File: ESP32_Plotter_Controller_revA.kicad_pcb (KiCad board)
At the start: 2 copper layers, 99.1 x 55.4 mm, 40 parts, among them J1 ARM JTAG 10pin, J10 Pen Lift, J11 Vselect, J12 X Motor, J13 Y Motor, J14 Neo Pixel LEDs, J15 Pen Direction, J16 Aux Port (I2C), J2 Power, J3 5V Aux, J4 Vin Aux, J5 Limit Switches, J6 Aux Port (SPI), J7 X Limit, J8 Micro_SD_Card, J9 Y Limit, U1 ESP-DEVKITC, U2 TMC2130, U3 TMC2130, U4 XL1509

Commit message: Update ESP32_Plotter_Controller_revA.kicad_pcb
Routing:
- net /Vin: track 149.5 -> 177.8 mm
- net GND: vias 13 -> 14
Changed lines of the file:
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@@
     (thickness 1.6)
     (drawings 185)
-    (tracks 589)
+    (tracks 593)
     (zones 0)
     (modules 40)
@@
     (34 B.Paste user)
     (35 F.Paste user)
-    (36 B.SilkS user)
-    (37 F.SilkS user)
+    (36 B.SilkS user hide)
+    (37 F.SilkS user hide)
     (38 B.Mask user)
     (39 F.Mask user)
@@
   )
   (setup
-    (last_trace_width 0.25)
+    (last_trace_width 0.5)
     (user_trace_width 0.5)
     (user_trace_width 0.6)
@@
   (via (at 29.718 101.854) (size 0.8) (drill 0.4) (layers F.Cu B.Cu) (net 1))
   (via (at 29.718 104.14) (size 0.8) (drill 0.4) (layers F.Cu B.Cu) (net 1))
-  (segment (start 36.068 94.742) (end 36.068 93.5667) (width 0.25) (layer B.Cu) (net 1) (status 1000000))
-  (segment (start 36.068 93.5667) (end 35.7006 93.5667) (width 0.25) (layer B.Cu) (net 1) (status 1000000))
-  (segment (start 35.7006 93.5667) (end 34.8897 92.7558) (width 0.25) (layer B.Cu) (net 1) (status 1000000))
-  (segment (start 35.7006 81.9473) (end 36.068 81.9473) (width 0.25) (layer B.Cu) (net 1) (status 1000000))
-  (segment (start 34.8897 82.7582) (end 35.7006 81.9473) (width 0.25) (layer B.Cu) (net 1) (status 1000000))
-  (segment (start 34.8897 92.7558) (end 34.8897 82.7582) (width 0.25) (layer B.Cu) (net 1) (status 1000000))
+  (segment (start 36.068 94.742) (end 36.068 93.5667) (width 0.25) (layer B.Cu) (net 1))
+  (segment (start 36.068 93.5667) (end 35.7006 93.5667) (width 0.25) (layer B.Cu) (net 1))
+  (segment (start 35.7006 93.5667) (end 34.8897 92.7558) (width 0.25) (layer B.Cu) (net 1))
+  (segment (start 35.7006 81.9473) (end 36.068 81.9473) (width 0.25) (layer B.Cu) (net 1))
+  (segment (start 34.8897 82.7582) (end 35.7006 81.9473) (width 0.25) (layer B.Cu) (net 1))
+  (segment (start 34.8897 92.7558) (end 34.8897 82.7582) (width 0.25) (layer B.Cu) (net 1))
+  (via (at 88.265 88.9) (size 0.8) (drill 0.4) (layers F.Cu B.Cu) (net 1))
   (segment (start 54.102 79.756) (end 52.9267 79.756) (width 0.25) (layer B.Cu) (net 2))
   (segment (start 39.878 86.4396) (end 47.7385 86.4396) (width 0.25) (layer B.Cu) (net 2))
@@
   (segment (start 60.628 105.349) (end 60.0955 104.8165) (width 0.75) (layer F.Cu) (net 34))
   (segment (start 61.595 105.349) (end 60.628 105.349) (width 0.75) (layer F.Cu) (net 34))
-  (segment (start 38.0181 113.1119) (end 39.37 111.76) (width 0.75) (layer F.Cu) (net 34))
-  (segment (start 39.37 111.76) (end 39.37 103.124) (width 0.75) (layer F.Cu) (net 34))
-  (segment (start 37.338 113.792) (end 38.0181 113.1119) (width 0.75) (layer F.Cu) (net 34))
   (segment (start 60.0955 104.8165) (end 60.0205 104.8165) (width 0.25) (layer F.Cu) (net 34))
   (segment (start 60.0205 104.8165) (end 59.563 104.359) (width 0.25) (layer F.Cu) (net 34))
@@
   (segment (start 67.691 83.693) (end 67.691 89.1518) (width 0.75) (layer F.Cu) (net 34))
   (segment (start 67.691 89.1518) (end 67.7822 89.243) (width 0.75) (layer F.Cu) (net 34))
-  (segment (start 46.355 83.693) (end 46.355 89.3342) (width 0.75) (layer F.Cu) (net 34))
-  (segment (start 46.355 89.3342) (end 45.7132 89.976) (width 0.75) (layer F.Cu) (net 34))
   (segment (start 46.355 83.693) (end 42.799 83.693) (width 0.5) (layer F.Cu) (net 34))
   (segment (start 42.799 83.693) (end 39.878 80.772) (width 0.5) (layer F.Cu) (net 34))
@@
   (segment (start 65.6072 91.418) (end 67.7822 89.243) (width 0.75) (layer F.Cu) (net 34))
   (segment (start 67.7822 89.243) (end 73.081 89.243) (width 0.75) (layer F.Cu) (net 34))
-  (segment (start 73.081 89.243) (end 73.881 90.043) (width 0.75) (layer F.Cu) (net 34))
-  (segment (start 39.37 103.124) (end 44.196 98.298) (width 0.75) (layer F.Cu) (net 34))
-  (segment (start 44.196 98.298) (end 44.196 91.4932) (width 0.75) (layer F.Cu) (net 34))
-  (segment (start 44.196 91.4932) (end 45.7132 89.976) (width 0.75) (layer F.Cu) (net 34))
-  (segment (start 45.7132 89.976) (end 53.748 89.976) (width 0.75) (layer F.Cu) (net 34))
-  (segment (start 53.748 89.976) (end 53.815 90.043) (width 0.75) (layer F.Cu) (net 34))
-  (segment (start 39.37 103.124) (end 45.53 103.124) (width 0.75) (layer F.Cu) (net 34))
-  (segment (start 45.53 103.124) (end 47.498 101.156) (width 0.75) (layer F.Cu) (net 34))
   (segment (start 61.11669 115.66731) (end 62.992 113.792) (width 0.75) (layer F.Cu) (net 34))
   (segment (start 39.21331 115.66731) (end 61.11669 115.66731) (width 0.75) (layer F.Cu) (net 34))
@@
   (segment (start 65.84931 116.14131) (end 82.35969 116.14131) (width 0.75) (layer F.Cu) (net 34))
   (segment (start 63.5 113.792) (end 65.84931 116.14131) (width 0.75) (layer F.Cu) (net 34))
+  (segment (start 73.081 89.243) (end 73.881 90.043) (width 0.8) (layer F.Cu) (net 34))
+  (segment (start 67.745238 89.243) (end 73.081 89.243) (width 0.8) (layer F.Cu) (net 34))
+  (segment (start 65.545228 91.44301) (end 67.745238 89.243) (width 0.8) (layer F.Cu) (net 34))
+  (segment (start 55.21501 91.44301) (end 65.545228 91.44301) (width 0.8) (layer F.Cu) (net 34))
+  (segment (start 53.815 90.043) (end 55.21501 91.44301) (width 0.8) (layer F.Cu) (net 34))
+  (segment (start 67.745238 83.747238) (end 67.691 83.693) (width 0.8) (layer F.Cu) (net 34))
+  (segment (start 67.745238 89.243) (end 67.745238 83.747238) (width 0.8) (layer F.Cu) (net 34))
+  (segment (start 39.37 111.76) (end 39.37 103.124) (width 1) (layer F.Cu) (net 34))
+  (segment (start 37.338 113.792) (end 39.37 111.76) (width 1) (layer F.Cu) (net 34))
+  (segment (start 44.892999 85.155001) (end 46.355 83.693) (width 1) (layer F.Cu) (net 34))
+  (segment (start 44.892999 97.601001) (end 44.892999 85.155001) (width 1) (layer F.Cu) (net 34))
+  (segment (start 39.37 103.124) (end 44.892999 97.601001) (width 1) (layer F.Cu) (net 34))
+  (segment (start 52.705 90.043) (end 53.815 90.043) (width 1) (layer F.Cu) (net 34))
+  (segment (start 46.355 83.693) (end 52.705 90.043) (width 1) (layer F.Cu) (net 34))
+  (segment (start 45.53 103.124) (end 47.498 101.156) (width 1) (layer F.Cu) (net 34))
+  (segment (start 39.37 103.124) (end 45.53 103.124) (width 1) (layer F.Cu) (net 34))
   (segment (start 85.471 96.393) (end 90.424 91.44) (width 0.25) (layer B.Cu) (net 38))
   (segment (start 90.424 91.44) (end 95.885 91.44) (width 0.25) (layer B.Cu) (net 38))

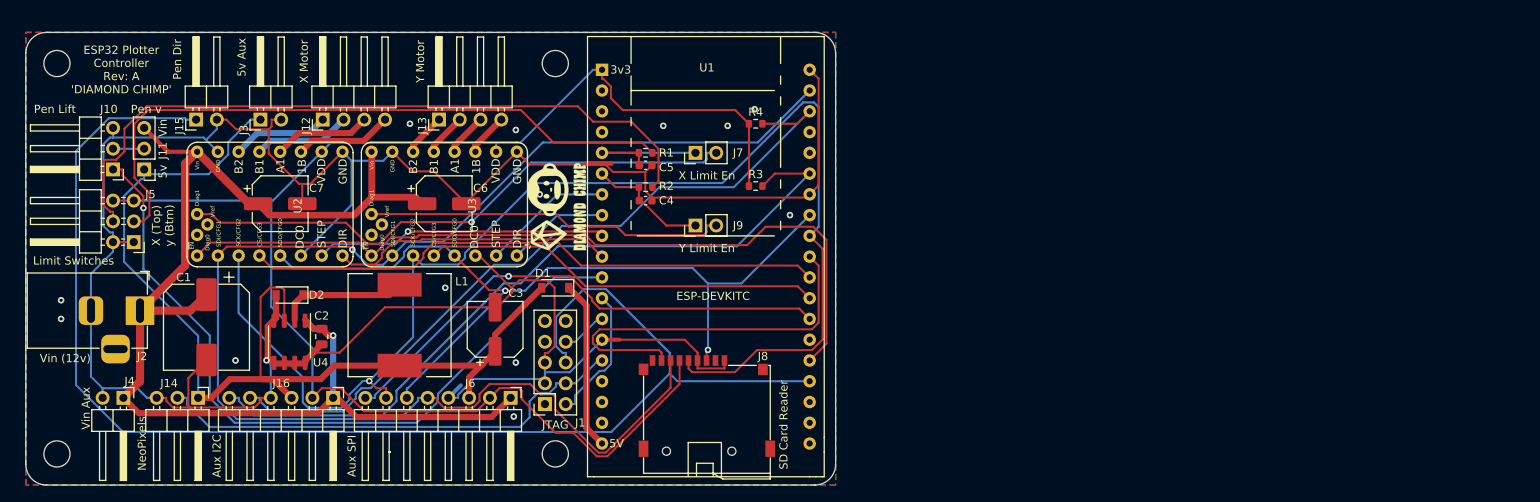
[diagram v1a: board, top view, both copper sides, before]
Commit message: Fix DCDC track layout
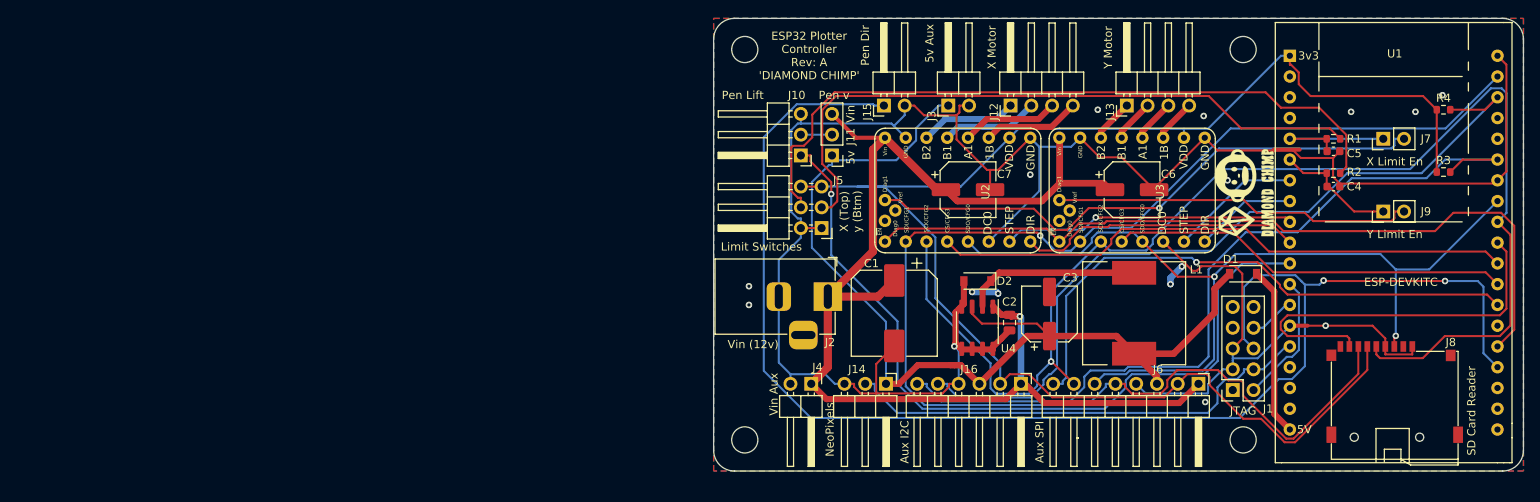
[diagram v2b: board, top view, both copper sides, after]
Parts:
- moved L1 89.9 mm to (161.0, 103.4)
- moved C1 84.2 mm to (131.6, 103.4)
- moved C4 84.2 mm to (185.4, 87.9)
- moved C5 84.2 mm to (185.4, 83.6)
- moved J16 84.2 mm to (147.1, 112.1)
- moved J5 84.2 mm to (122.7, 93.0)
- moved R1 84.2 mm to (185.4, 82.1)
- moved R2 84.2 mm to (185.4, 86.3)
- moved U2 84.2 mm to (130.5, 94.7)
- moved C6 84.2 mm to (160.7, 88.3)
- moved C7 84.2 mm to (140.7, 88.3)
- moved D1 84.2 mm to (174.3, 98.6)
- moved D2 84.2 mm to (141.8, 99.5)
- moved G*** 84.2 mm to (174.3, 88.7)
- moved H2 84.2 mm to (174.3, 71.2)
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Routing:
- net GND: track 330.3 -> 306.9 mm, vias 14 -> 16
- net /MISO: track 102.2 -> 110.4 mm
- net /PEN_DIR_JTAG_TDO: track 167.9 -> 175.7 mm, vias 0 -> 2
- net +3V3: track 181.9 -> 189.0 mm
- net /CS_AUX: track 63.0 -> 69.3 mm
- net /SDA: track 91.5 -> 97.8 mm
- net Net-(D2-Pad1): track 15.9 -> 21.5 mm
- net /PEN_LIFT: track 90.7 -> 95.9 mm
- net +5V: track 126.5 -> 121.4 mm
- net /SCL: track 91.3 -> 96.4 mm
- net /JTAG_TMS: track 16.7 -> 16.1 mm
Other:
- board text added: "github.com/markjb/ESP32_Plotter_Controller"
- board text removed: "URL: github.com/markjb/ESP32_Plotter_Controller"
